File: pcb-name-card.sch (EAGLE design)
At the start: 10 parts, among them IC1 NTAG21XFDRC-FIT, IC2 NT3H1X01W0FTT, U1 3V, U2 3V

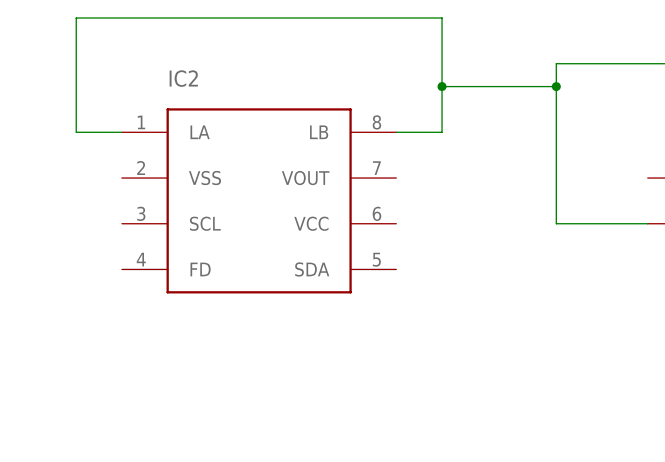
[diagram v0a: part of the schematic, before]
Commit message: NFC harvesting test points
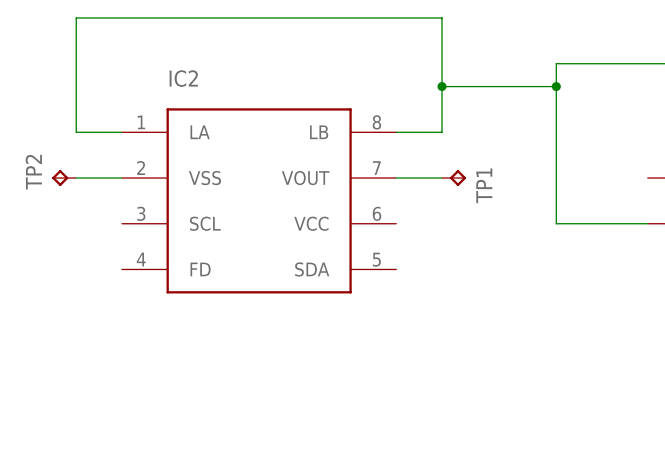
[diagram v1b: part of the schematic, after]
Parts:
- added TP1: VOUT, testpad:TPB2,54
- added TP2: GND, testpad:TPB2,54
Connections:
- new net N$10: IC2.VSS, TP2.TP
- new net N$93: IC2.VOUT, TP1.TP
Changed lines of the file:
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@@
 <part name="IC2" library="ntagi2c" deviceset="NT3H1X01" device="W0FTT"/>
 <part name="IC1" library="ntag21xf" deviceset="NTAG21XF" device="DRC-FIT"/>
+<part name="TP1" library="testpad" deviceset="TP" device="B2,54" value="VOUT"/>
+<part name="TP2" library="testpad" deviceset="TP" device="B2,54" value="GND"/>
 </parts>
 <sheets>
@@
 <instance part="IC2" gate="G$1" x="27.94" y="142.24"/>
 <instance part="IC1" gate="G$1" x="83.82" y="142.24"/>
+<instance part="TP1" gate="G$1" x="50.8" y="144.78" rot="R270"/>
+<instance part="TP2" gate="G$1" x="5.08" y="144.78" rot="R90"/>
 </instances>
 <busses>
@@
 </segment>
 </net>
+<net name="N$10" class="0">
+<segment>
+<pinref part="IC2" gate="G$1" pin="VSS"/>
+<pinref part="TP2" gate="G$1" pin="TP"/>
+<wire x1="12.7" y1="144.78" x2="7.62" y2="144.78" width="0.1524" layer="91"/>
+</segment>
+</net>
+<net name="N$93" class="0">
+<segment>
+<pinref part="IC2" gate="G$1" pin="VOUT"/>
+<pinref part="TP1" gate="G$1" pin="TP"/>
+<wire x1="43.18" y1="144.78" x2="48.26" y2="144.78" width="0.1524" layer="91"/>
+</segment>
+</net>
